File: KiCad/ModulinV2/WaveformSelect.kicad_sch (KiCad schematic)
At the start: 72 parts, among them IC24 NC7SZ74K8X, IC25 SN74AHCT1G00DBVR, IC26 SN74AHCT1G00DBVR, IC27 SN74AHCT1G00DBVR, IC28 SN74AHC1G02DBVR, IC29 SN74AHC1G02DBVR, IC30 SN74HC193DR, IC31 TMUX4052DYYR, IC32 TMUX4051DYYRQ1, IC33 TMUX4051DYYRQ1, J5 TSW-104-07-T-D, J6 TSW-104-07-T-D, J7 TSW-104-07-T-D, J8 TSW-104-07-T-D, U1 SN74AHC1G08DBVR

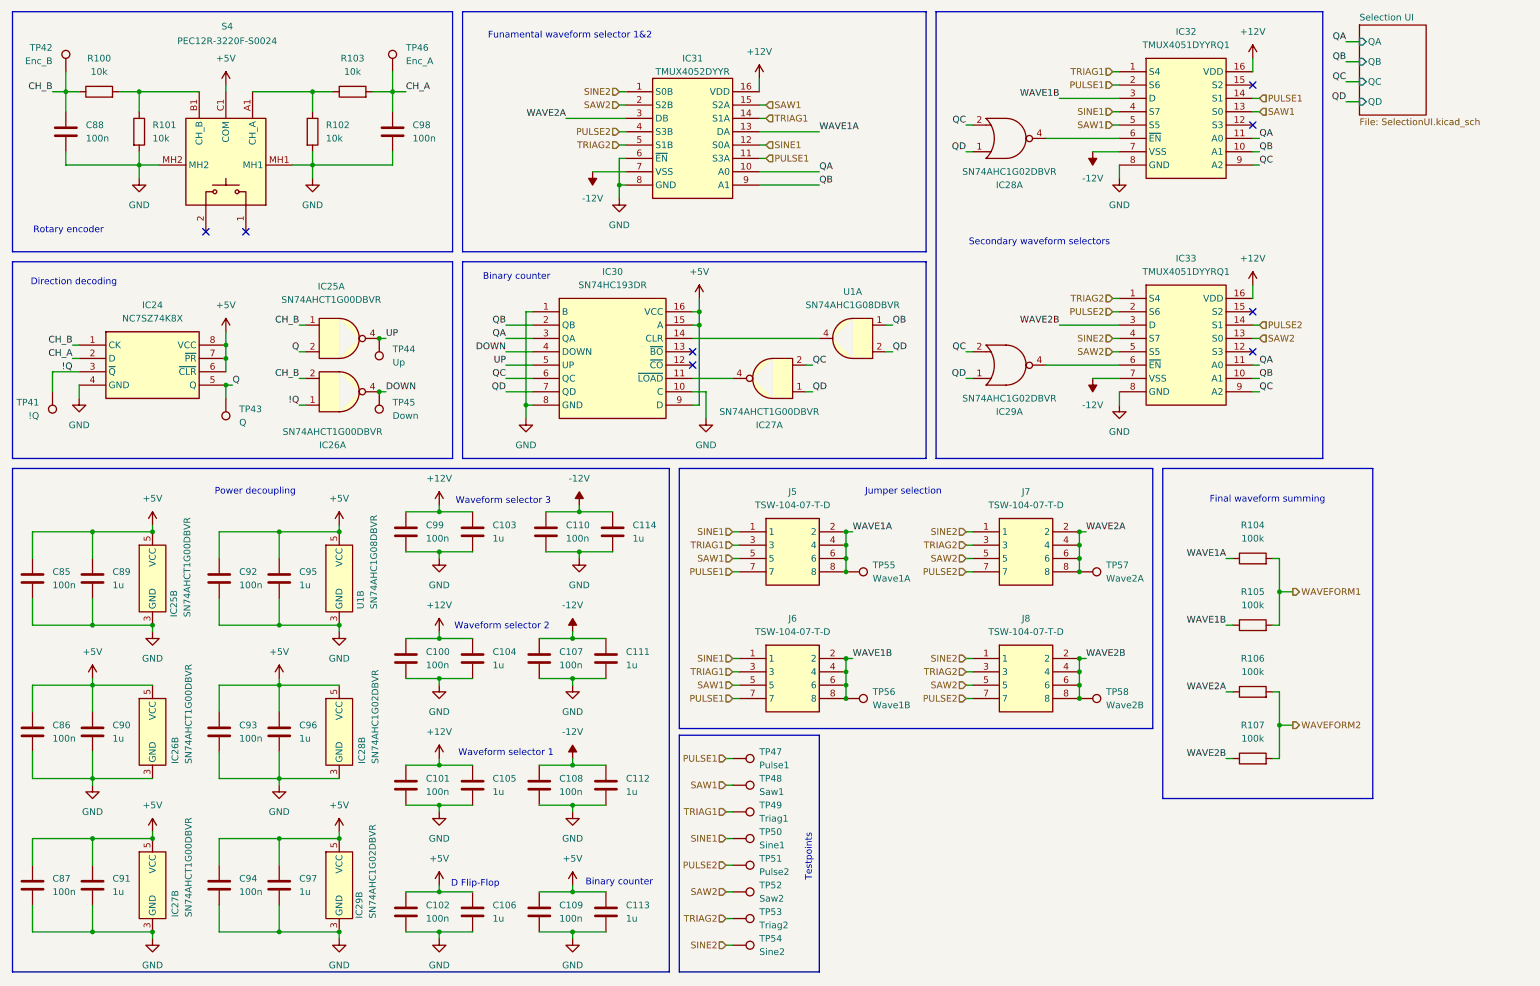
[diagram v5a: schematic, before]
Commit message: Completed tuning & mod wheel layouts
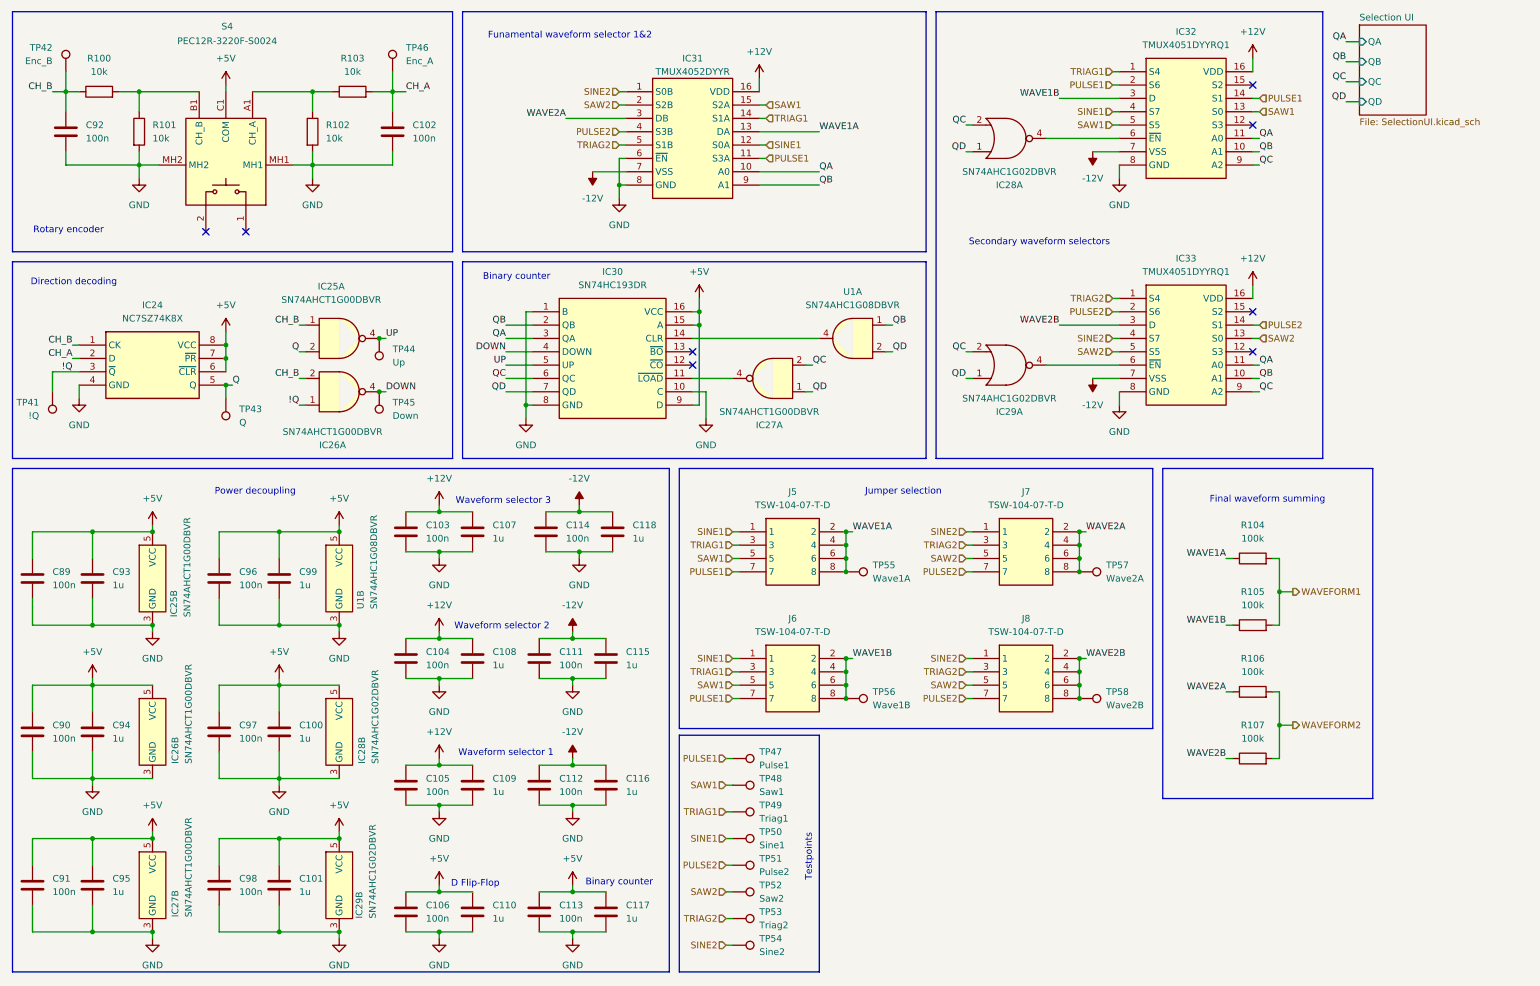
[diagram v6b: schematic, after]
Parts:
- renumbered C96 to C100, C97 to C101, C98 to C102, C99 to C103, C100 to C104, C101 to C105, C102 to C106, C103 to C107, C104 to C108, C105 to C109, C106 to C110, C107 to C111, C108 to C112, C109 to C113, C110 to C114, C111 to C115, C112 to C116, C113 to C117, C114 to C118, C85 to C89, C86 to C90, C87 to C91, C88 to C92, C89 to C93, C90 to C94, C91 to C95, C92 to C96, C93 to C97, C94 to C98, C95 to C99

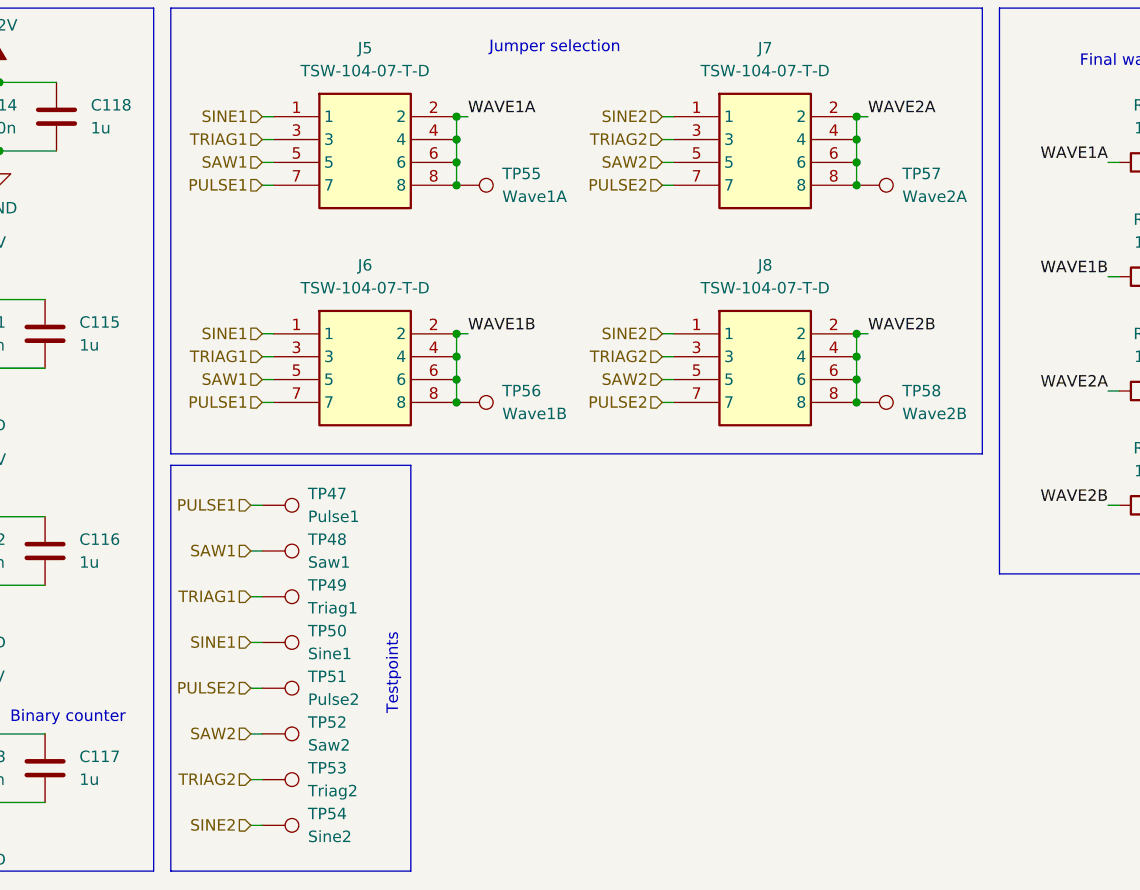
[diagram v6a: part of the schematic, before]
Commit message: Completed ADSR layout, started with Waveform select
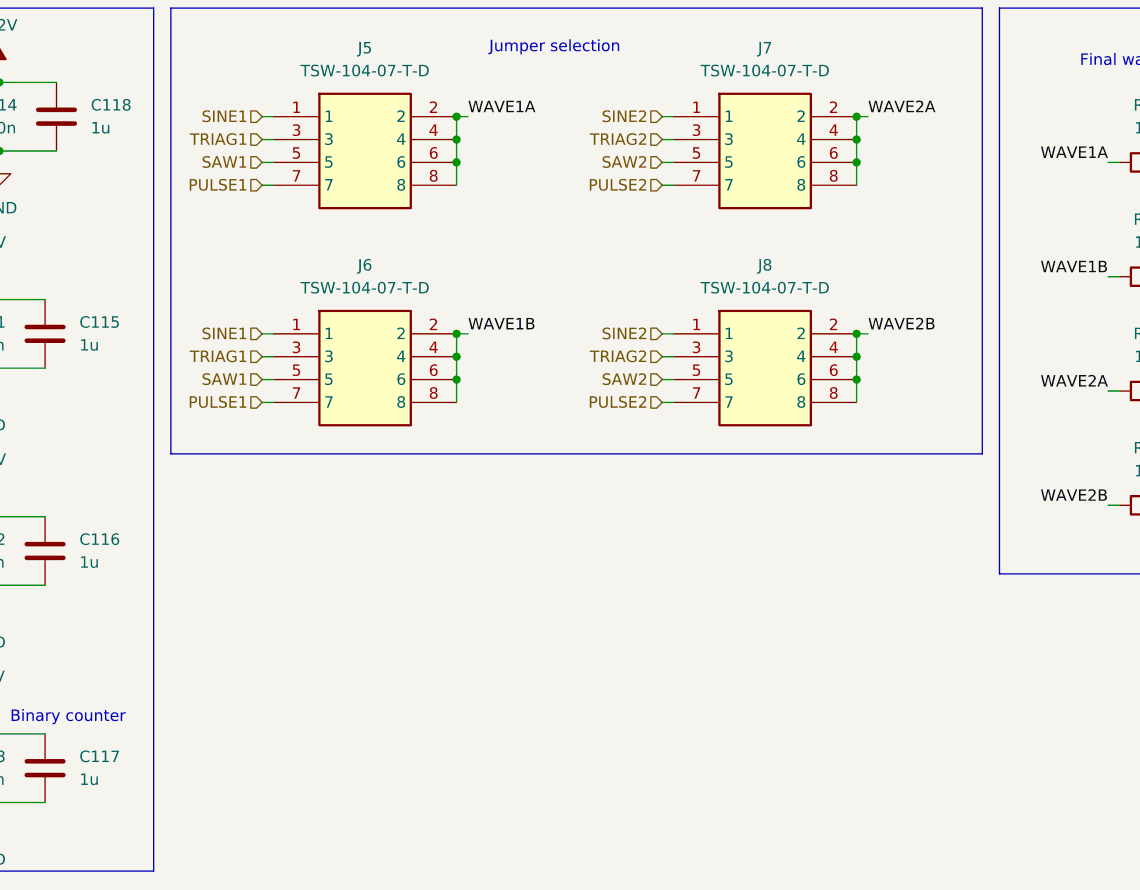
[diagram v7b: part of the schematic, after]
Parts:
- removed TP47: Pulse1, SamacSys_Parts:TestPointLoop, symbol Connector:TestPoint
- removed TP48: Saw1, SamacSys_Parts:TestPointLoop, symbol Connector:TestPoint
- removed TP49: Triag1, SamacSys_Parts:TestPointLoop, symbol Connector:TestPoint
- removed TP50: Sine1, SamacSys_Parts:TestPointLoop, symbol Connector:TestPoint
- removed TP51: Pulse2, SamacSys_Parts:TestPointLoop, symbol Connector:TestPoint
- removed TP52: Saw2, SamacSys_Parts:TestPointLoop, symbol Connector:TestPoint
- removed TP53: Triag2, SamacSys_Parts:TestPointLoop, symbol Connector:TestPoint
- removed TP54: Sine2, SamacSys_Parts:TestPointLoop, symbol Connector:TestPoint
- removed TP55: Wave1A, SamacSys_Parts:TestPointLoop, symbol Connector:TestPoint
- removed TP56: Wave1B, SamacSys_Parts:TestPointLoop, symbol Connector:TestPoint
- removed TP57: Wave2A, SamacSys_Parts:TestPointLoop, symbol Connector:TestPoint
- removed TP58: Wave2B, SamacSys_Parts:TestPointLoop, symbol Connector:TestPoint
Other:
- note removed: "Testpoints"

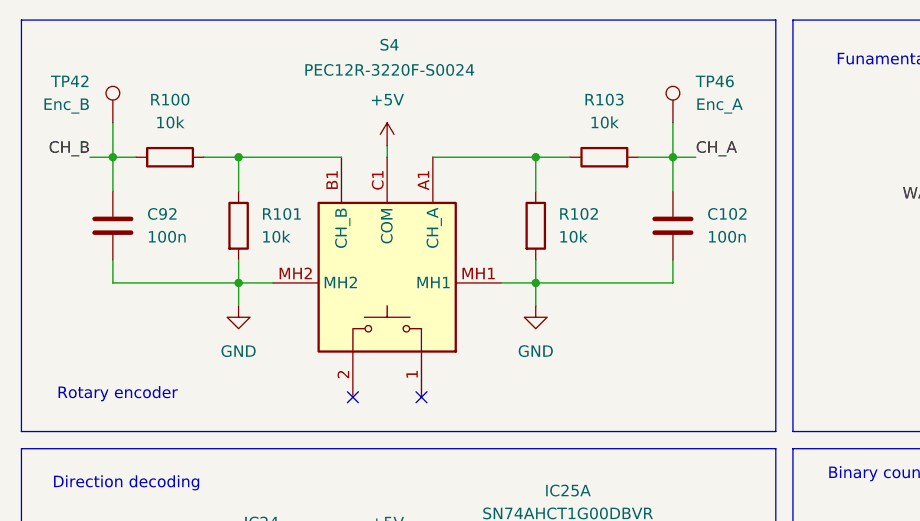
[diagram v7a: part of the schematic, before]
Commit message: Fixed schematic connections
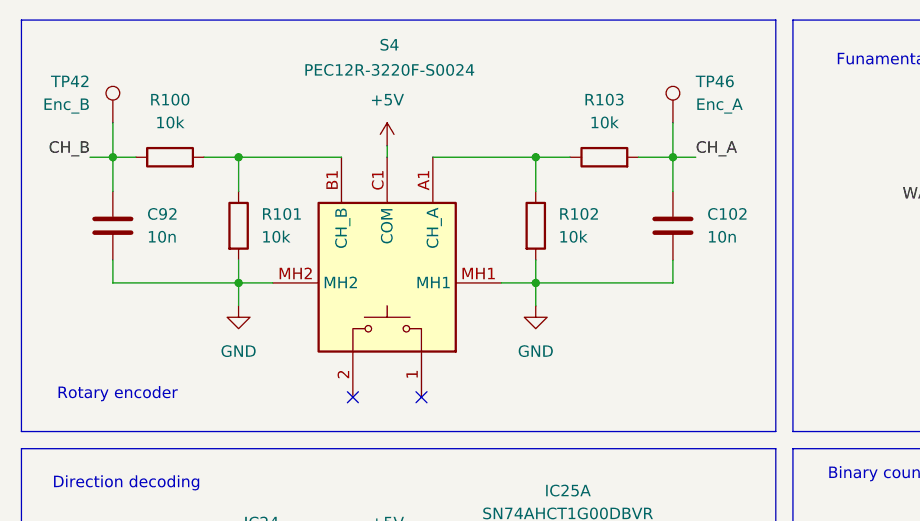
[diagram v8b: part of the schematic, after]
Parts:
- C102, C92: value 100n -> 10n
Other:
- company: (none) -> TalTech
- title: Octave Selector -> Waveform selector
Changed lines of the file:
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@@
 	(paper "A4")
 	(title_block
-		(title "Octave Selector")
-		(date "2025-07-13")
+		(title "Waveform selector")
+		(date "2026-04-29")
+		(rev "1.4")
+		(company "TalTech")
 		(comment 1 "Instructor: Kaiser Pärnamets")
-		(comment 2 "By: Rasmus Palk")
+		(comment 2 "Author: Rasmus Palk")
 	)
 	(rectangle
@@
 			)
 		)
-		(property "Value" "100n"
+		(property "Value" "10n"
 			(at 27.94 38.0999 0)
 			(effects
@@
 			)
 		)
-		(property "Value" "100n"
+		(property "Value" "10n"
 			(at 90.17 38.0999 0)
 			(effects
